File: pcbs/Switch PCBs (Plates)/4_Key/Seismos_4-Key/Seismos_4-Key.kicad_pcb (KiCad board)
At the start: 2 copper layers, 19 x 86.4 mm, 12 parts, among them J1 SM10B-SRSS-TB(LF)(SN), SW1 Switch_SK6812-E_Diode, SW2 Switch_SK6812-E_Diode, SW3 Switch_SK6812-E_Diode, SW4 Switch_SK6812-E_Diode

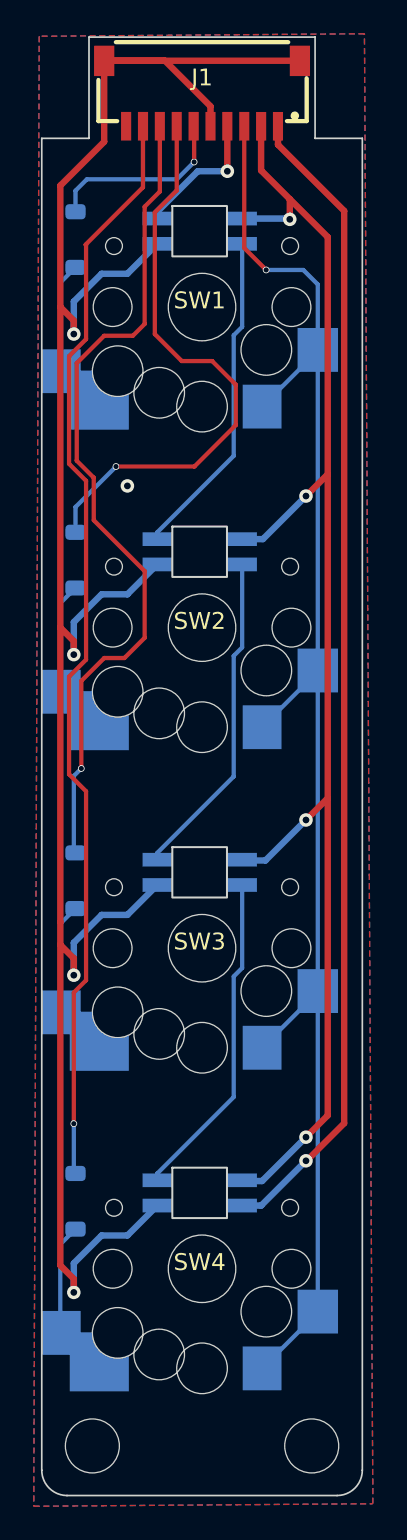
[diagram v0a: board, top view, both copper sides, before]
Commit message: Added stencils for new and old PCBs
Created stencils for solder pasting PCBs with the core and plates.
I ordered both new and old versions so two stencils were made; however,
the holes for the old variant are misaligned. For this, use the other
aligning holes.

In addition, repaired footprints for switches where the switch footprint
was appearing on the reverse side. This is now fixed.
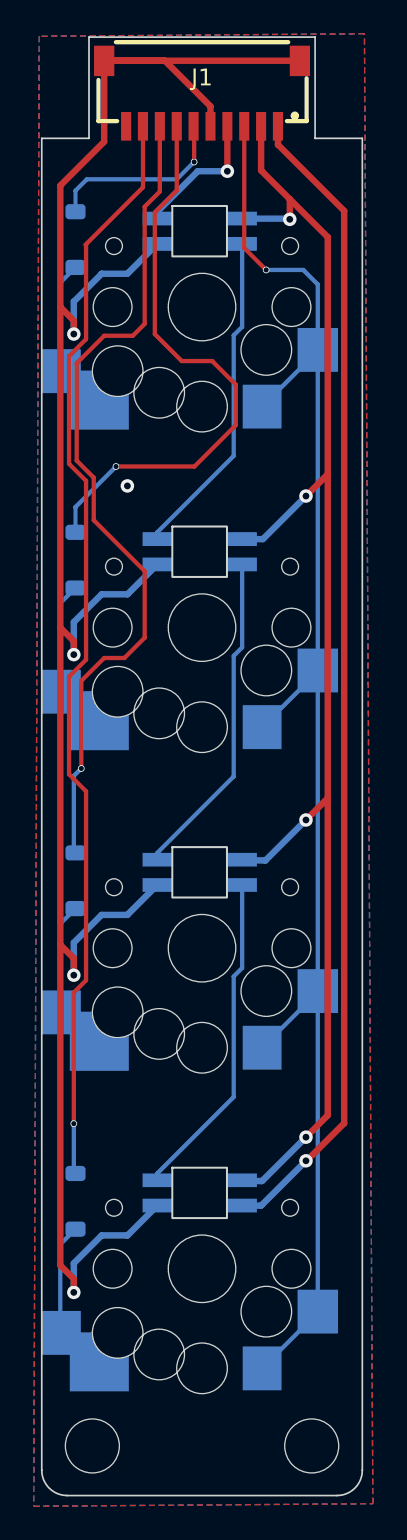
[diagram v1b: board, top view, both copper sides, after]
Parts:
- SW1, SW2, SW3, SW4: moved to B.Cu
- turned SW1 to 180 degrees
- turned SW2 to 180 degrees
- turned SW3 to 180 degrees
- turned SW4 to 180 degrees

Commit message: Release v1.1
***NOTE***: If you have a previous commit, please update your files.
This commit fixes the incorrect RGB pinout and power switch as the
RGB footprint was incorrect.
The power switch behaviour is also fixed in this commit so the position
matches on both sides.
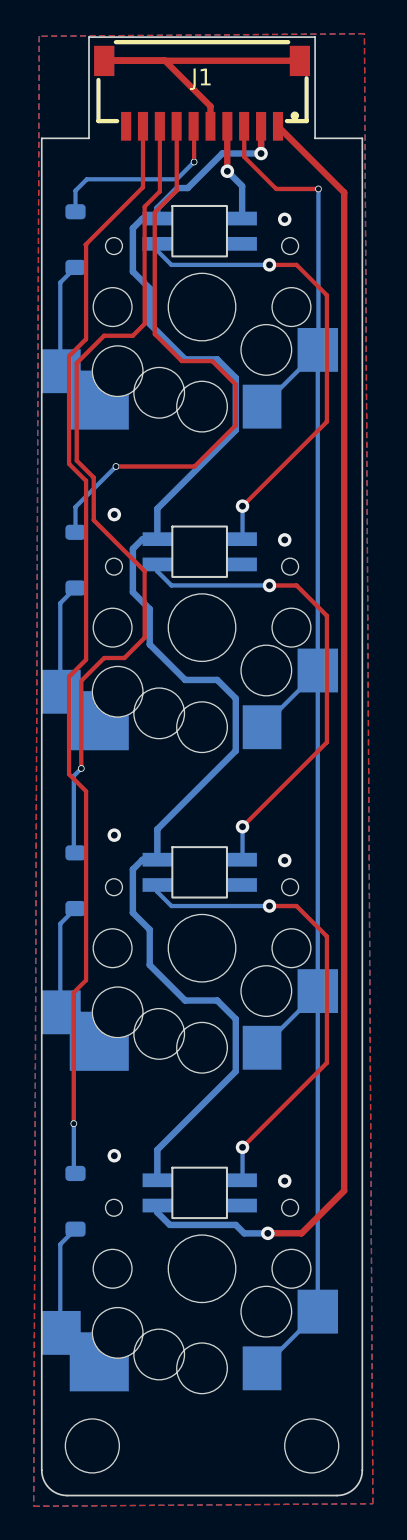
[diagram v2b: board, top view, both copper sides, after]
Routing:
- net GND: track 131.5 -> 18.7 mm, vias 5 -> 7
- net /RGB_Out: track 68.8 -> 77.8 mm
- net Net-(SW3B-DOUT): track 19.6 -> 28.1 mm, vias 0 -> 2
- net Net-(SW2B-DOUT): track 19.6 -> 28.1 mm, vias 0 -> 2
- net Net-(SW1B-DOUT): track 19.6 -> 28.1 mm, vias 0 -> 2
- net /V+: track 84.2 -> 86.8 mm, vias 4 -> 1
- net /RGB_In: track 8.22 -> 5.83 mm
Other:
- board text added: "Rev. 1.1"
- board text removed: "Rev. 1.0"
